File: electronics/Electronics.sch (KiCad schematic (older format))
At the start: 34 parts, among them U1 DRV8243, U2 DRV8243, U3 DRV8243

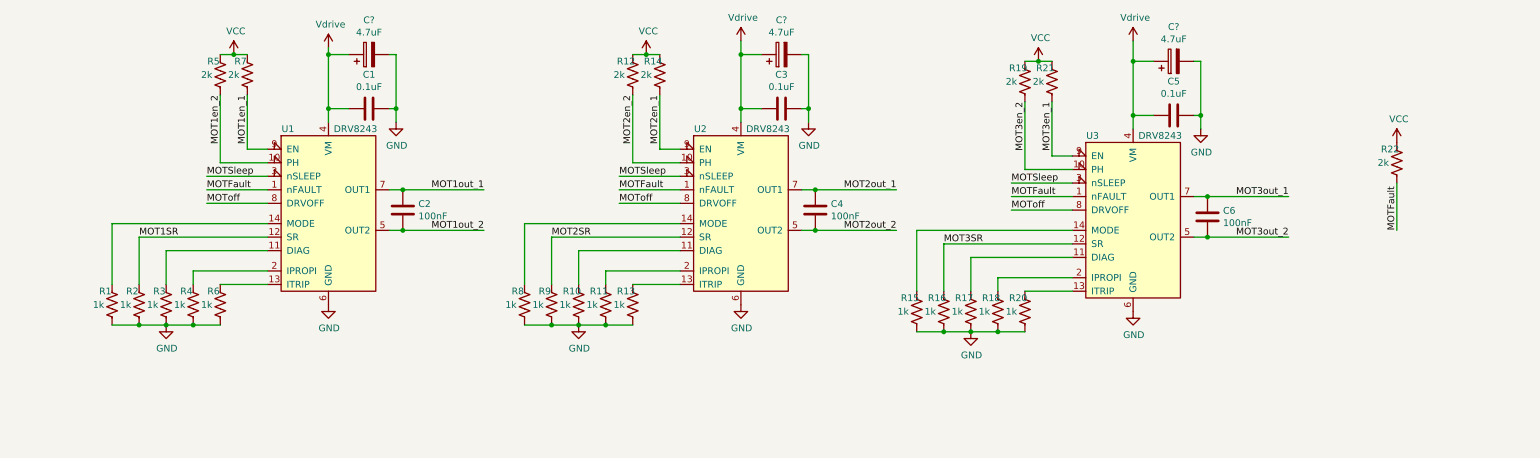
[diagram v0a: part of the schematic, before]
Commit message: Updated and removed unnecessary resistors, removed cache
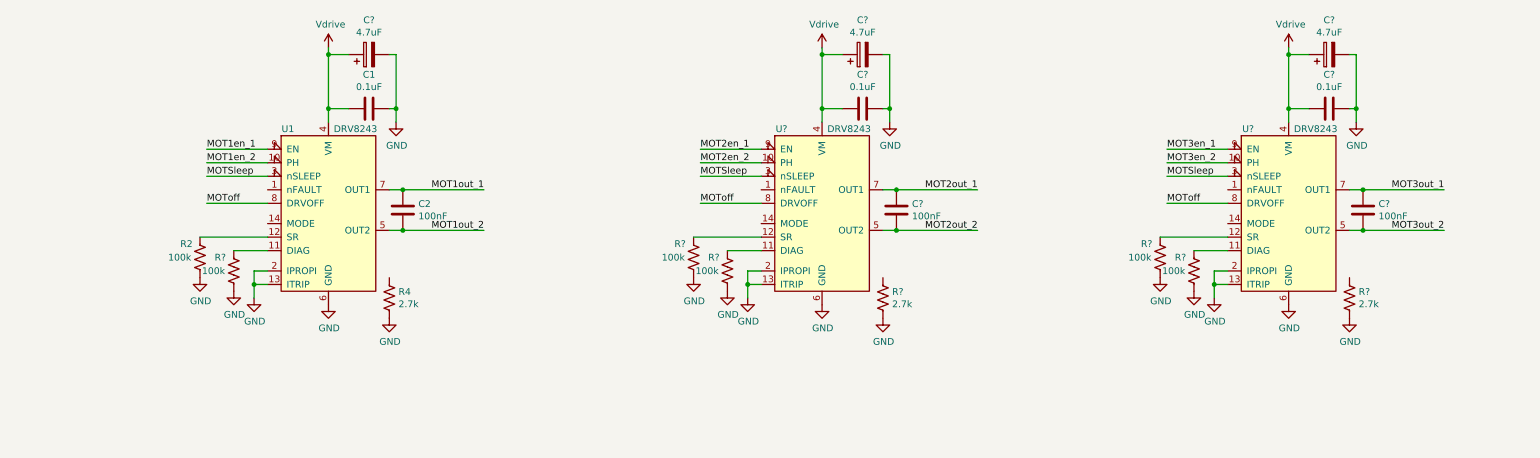
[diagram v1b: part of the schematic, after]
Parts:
- removed C3, C5: 0.1uF, Resistor_SMD:R_0603_1608Metric_Pad0.98x0.95mm_HandSolder, symbol Device:C
- removed C4, C6: 100nF, Resistor_SMD:R_0603_1608Metric_Pad0.98x0.95mm_HandSolder, symbol Device:C
- removed C? (x2): 4.7uF, symbol Device:CP
- removed R1, R10, R11, R13, R15, R16, R17, R18, R20, R3, R6, R8, R9: 1k, Resistor_SMD:R_0603_1608Metric_Pad0.98x0.95mm_HandSolder, symbol Device:R_US
- removed R12, R14, R19, R21, R22, R5, R7: 2k, Resistor_SMD:R_0603_1608Metric_Pad0.98x0.95mm_HandSolder, symbol Device:R_US
- removed U2, U3: DRV8243, Electronics:VQFN-HR-14, symbol Electronics:DRV8243
- added C? (x2): 0.1uF, Capacitor_SMD:C_0603_1608Metric_Pad1.08x0.95mm_HandSolder, symbol Device:C
- added C? (x2): 100nF, Resistor_SMD:R_0603_1608Metric_Pad0.98x0.95mm_HandSolder, symbol Device:C
- added C? (x2): 4.7uF, symbol Device:CP
- added R? (x5): 100k, Resistor_SMD:R_0603_1608Metric_Pad0.98x0.95mm_HandSolder, symbol Device:R_US
- added R? (x2): 2.7k, Resistor_SMD:R_0603_1608Metric_Pad0.98x0.95mm_HandSolder, symbol Device:R_US
- added U? (x2): DRV8243, Electronics:VQFN-HR-14, symbol Electronics:DRV8243
- R2: value 1k -> 100k
- R4: value 1k -> 2.7k
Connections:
- net GND: now also U1.13 (ITRIP), U1.2 (IPROPI), C?.1, C?.1, C?.2, C?.2, R?.2, R?.2, R?.2, R?.2, R?.2, R?.2, R?.2, U?.13 (ITRIP), U?.13 (ITRIP), U?.2 (IPROPI), U?.2 (IPROPI), U?.6 (GND), U?.6 (GND)
- net MOT2en_1: now also U?.9 (EN)
- net MOT2en_2: now also U?.10 (PH)
- net MOT2out_1: now also C?.1, U?.7 (OUT1)
- net MOT2out_2: now also C?.2, U?.5 (OUT2)
- net MOT3en_1: now also U?.9 (EN)
- net MOT3en_2: now also U?.10 (PH)
- net MOT3out_1: now also C?.1, U?.7 (OUT1)
- net MOT3out_2: now also C?.2, U?.5 (OUT2)
- net MOTSleep: now also U?.3 (nSLEEP), U?.3 (nSLEEP)
- net MOToff: now also U?.8 (DRVOFF), U?.8 (DRVOFF)
- net Vdrive: now also C?.1, C?.1, C?.2, C?.2, U?.4 (VM), U?.4 (VM)
- net at U1.11 (DIAG): now also R?.1
- net at R4.1: no longer U1.2 (IPROPI)
- net MOT1SR: no longer names the net of R2.1, U1.12 (SR)
- net MOTFault: no longer names the net of U1.1 (nFAULT)
- new net: R?.1, U?.12 (SR) (x2)
- new net: R?.1, U?.11 (DIAG) (x2)
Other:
- moved on the sheet: R2, R4

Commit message: Reorganised schematics, added regulators
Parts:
- removed C1, C? (x2): 0.1uF, Capacitor_SMD:C_0603_1608Metric_Pad1.08x0.95mm_HandSolder, symbol Device:C
- removed C2, C? (x2): 100nF, Resistor_SMD:R_0603_1608Metric_Pad0.98x0.95mm_HandSolder, symbol Device:C
- removed C? (x3): 4.7uF, symbol Device:CP
- removed R2, R? (x5): 100k, Resistor_SMD:R_0603_1608Metric_Pad0.98x0.95mm_HandSolder, symbol Device:R_US
- removed R4, R? (x2): 2.7k, Resistor_SMD:R_0603_1608Metric_Pad0.98x0.95mm_HandSolder, symbol Device:R_US
- removed U1, U? (x2): DRV8243, Electronics:VQFN-HR-14, symbol Electronics:DRV8243

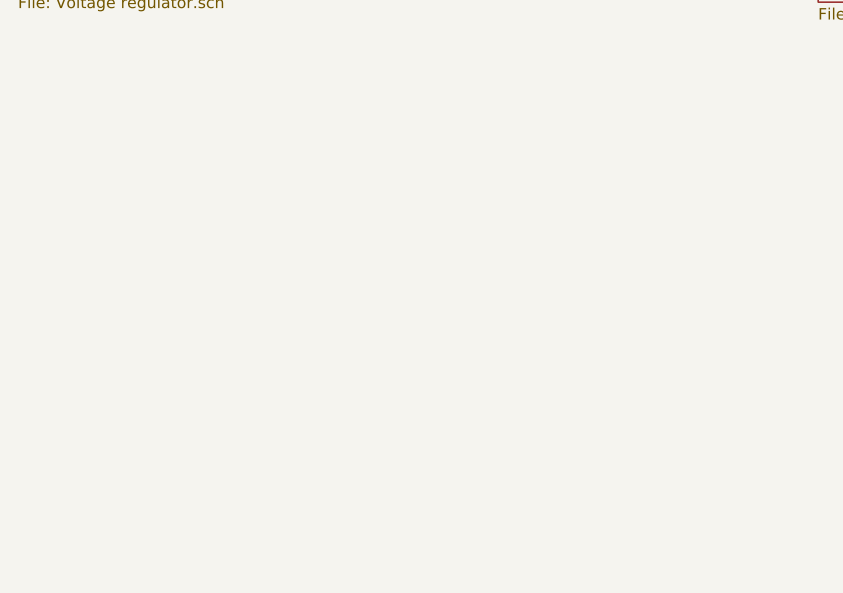
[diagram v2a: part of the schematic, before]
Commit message: Added connectors, started relabeling pins
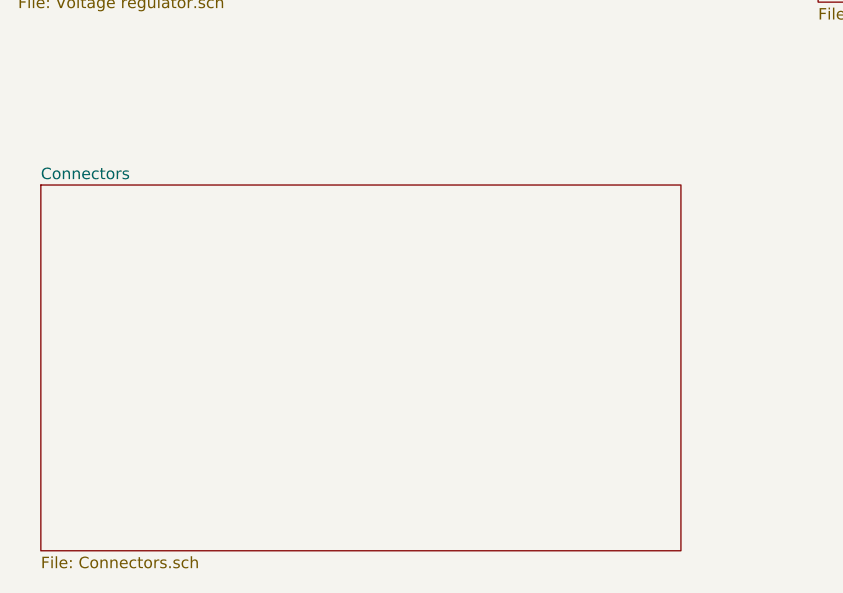
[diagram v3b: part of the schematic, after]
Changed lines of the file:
@@
 $Descr A4 11693 8268
 encoding utf-8
-Sheet 1 4
+Sheet 1 5
 Title ""
 Date ""
@@
 F1 "Voltage regulator.sch" 50
 $EndSheet
+$Sheet
+S 900  3650 2800 1600
+U 617B7795
+F0 "Connectors" 50
+F1 "Connectors.sch" 50
+$EndSheet
 $EndSCHEMATC

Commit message: Another restructure, added CPU pins, updated V regulators
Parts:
- added C? (x8): 0.1uF, symbol Device:C
- added C?: 4.7uF, symbol Device:CP
- added U?: STM32G441KBT3, LQFP32_7X7_STM, symbol 2021-09-13_09-53-18:STM32G441KBT3
- added U? (x3): MAX14930DASE+, 21-0041_S16+1_MXM, symbol MAX14930DASE+:MAX14930DASE+
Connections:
- net labels added: +3V3, +5VD, Aim-serv_PWM, Earth, GND, Hold-serv_PWM, MCU-Aim-serv_PWM, MCU-Hold-serv_PWM, MCU-MOT1en1, MCU-MOT1en2, MCU-MOT2en1, MCU-MOT2en2, MCU-MOT3en1, MCU-MOT3en2, MCU-TRW_PWM, MCU-USB_DM, MCU-USB_DP, MCU-mot1-enc_1, MCU-mot1-enc_2, MCU-mot2-enc_1, MCU-mot2-enc_2, MCU-mot3-enc_1, MCU-mot3-enc_2, MCU-mot_off, MCU-mot_sleep, MCU_NRST, MCU_SWCLK, MCU_SWDIO, MOT1en_1, MOT1en_2, MOT2en_1, MOT2en_2, MOT3en_1, MOT3en_2, MOT_off, MOT_sleep, TRW_PWM
- wire segments 0 -> 77

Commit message: Updated titles
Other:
- note added: "1.0"
- note added: "21/10/2021"
- note added: "CPU and isolators"
- note added: "Link to Hbridges"
- note added: "Link to all connectors and voltage regulators"
- note added: "Motor 1 and 2 PWM isolator"
- note added: "Motor 3 PWM, DC motors sleep and off control isolator"
- note added: "STM32G4 MCU"
- note added: "Thrower and servo control PWM isolator"
- moved on the sheet: C?

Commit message: Added debug LEDs
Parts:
- added D? (x2): RED_LED, symbol Device:LED
- added D? (x2): GREEN_LED, symbol Device:LED
- added R? (x4): 3.3k, symbol Device:R
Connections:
- net labels added: MCU-MOT1en_1, MCU-MOT1en_2, MCU-MOT2en_1, MCU-MOT2en_2, MCU-MOT3en_1, MCU-MOT3en_2, MCU-debug-LED_1, MCU-debug-LED_2, MCU-debug-LED_3, MCU-debug-LED_4
- net labels removed: MCU-MOT1en1, MCU-MOT1en2, MCU-MOT2en1, MCU-MOT2en2, MCU-MOT3en1, MCU-MOT3en2
- wire segments 77 -> 85
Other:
- note added: "Debug LED 1"
- note added: "Debug LED 2"
- note added: "Debug LED 3"
- note added: "Debug LED 4"

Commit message: Removed redundant comments
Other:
- note added: "Debug LEDs"
- note removed: "Debug LED 1"
- note removed: "Debug LED 2"
- note removed: "Debug LED 3"
- note removed: "Debug LED 4"
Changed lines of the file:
@@
 	0    1    1    0
 $EndComp
-Text Notes 1300 4950 0    50   ~ 0
-Debug LED 1
 $Comp
 L power:GND #PWR?
@@
 L Device:LED D?
 U 1 1 61754D02
-P 1700 5400
+P 1700 5250
 AR Path="/61754D02" Ref="D?"  Part="1"
 AR Path="/617B7795/61754D02" Ref="D?"  Part="1"
-F 0 "D?" H 1693 5145 50  0000 C CNN
-F 1 "RED_LED" H 1693 5236 50  0000 C CNN
-F 2 "" H 1700 5400 50  0001 C CNN
-F 3 "~" H 1700 5400 50  0001 C CNN
-	1    1700 5400
+F 0 "D?" H 1693 4995 50  0000 C CNN
+F 1 "RED_LED" H 1693 5086 50  0000 C CNN
+F 2 "" H 1700 5250 50  0001 C CNN
+F 3 "~" H 1700 5250 50  0001 C CNN
+	1    1700 5250
 	-1   0    0    1
 $EndComp
@@
 L Device:R R?
 U 1 1 61754D08
-P 2050 5400
+P 2050 5250
 AR Path="/615F51F3/61754D08" Ref="R?"  Part="1"
 AR Path="/617B7795/61754D08" Ref="R?"  Part="1"
 AR Path="/61754D08" Ref="R?"  Part="1"
-F 0 "R?" V 1800 5400 50  0000 C CNN
-F 1 "3.3k" V 1900 5400 50  0000 C CNN
-F 2 "" V 1980 5400 50  0001 C CNN
-F 3 "~" H 2050 5400 50  0001 C CNN
-	1    2050 5400
+F 0 "R?" V 1800 5250 50  0000 C CNN
+F 1 "3.3k" V 1900 5250 50  0000 C CNN
+F 2 "" V 1980 5250 50  0001 C CNN
+F 3 "~" H 2050 5250 50  0001 C CNN
+	1    2050 5250
 	0    1    1    0
 $EndComp
-Text Notes 1350 5650 0    50   ~ 0
-Debug LED 2
 $Comp
 L power:GND #PWR?
 U 1 1 61754D0F
-P 2200 5400
+P 2200 5250
 AR Path="/615F51F3/61754D0F" Ref="#PWR?"  Part="1"
 AR Path="/617B7795/61754D0F" Ref="#PWR?"  Part="1"
 AR Path="/61754D0F" Ref="#PWR?"  Part="1"
-F 0 "#PWR?" H 2200 5150 50  0001 C CNN
-F 1 "GND" H 2205 5227 50  0000 C CNN
-F 2 "" H 2200 5400 50  0001 C CNN
-F 3 "" H 2200 5400 50  0001 C CNN
-	1    2200 5400
+F 0 "#PWR?" H 2200 5000 50  0001 C CNN
+F 1 "GND" H 2205 5077 50  0000 C CNN
+F 2 "" H 2200 5250 50  0001 C CNN
+F 3 "" H 2200 5250 50  0001 C CNN
+	1    2200 5250
 	1    0    0    -1
 $EndComp
 Wire Wire Line
-	1850 5400 1900 5400
+	1850 5250 1900 5250
 $Comp
 L Device:LED D?
@@
 	0    1    1    0
 $EndComp
-Text Notes 2800 4950 0    50   ~ 0
-Debug LED 3
 $Comp
 L power:GND #PWR?
@@
 L Device:LED D?
 U 1 1 61778BA0
-P 3200 5400
+P 3200 5250
 AR Path="/61778BA0" Ref="D?"  Part="1"
 AR Path="/617B7795/61778BA0" Ref="D?"  Part="1"
-F 0 "D?" H 3193 5145 50  0000 C CNN
-F 1 "GREEN_LED" H 3193 5236 50  0000 C CNN
-F 2 "" H 3200 5400 50  0001 C CNN
-F 3 "~" H 3200 5400 50  0001 C CNN
-	1    3200 5400
+F 0 "D?" H 3193 4995 50  0000 C CNN
+F 1 "GREEN_LED" H 3193 5086 50  0000 C CNN
+F 2 "" H 3200 5250 50  0001 C CNN
+F 3 "~" H 3200 5250 50  0001 C CNN
+	1    3200 5250
 	-1   0    0    1
 $EndComp
@@
 L Device:R R?
 U 1 1 61778BA6
-P 3550 5400
+P 3550 5250
 AR Path="/615F51F3/61778BA6" Ref="R?"  Part="1"
 AR Path="/617B7795/61778BA6" Ref="R?"  Part="1"
 AR Path="/61778BA6" Ref="R?"  Part="1"
-F 0 "R?" V 3300 5400 50  0000 C CNN
-F 1 "3.3k" V 3400 5400 50  0000 C CNN
-F 2 "" V 3480 5400 50  0001 C CNN
-F 3 "~" H 3550 5400 50  0001 C CNN
-	1    3550 5400
+F 0 "R?" V 3300 5250 50  0000 C CNN
+F 1 "3.3k" V 3400 5250 50  0000 C CNN
+F 2 "" V 3480 5250 50  0001 C CNN
+F 3 "~" H 3550 5250 50  0001 C CNN
+	1    3550 5250
 	0    1    1    0
 $EndComp
-Text Notes 2800 5650 0    50   ~ 0
-Debug LED 4
+Text Notes 2050 5650 0    50   ~ 0
+Debug LEDs
 $Comp
 L power:GND #PWR?
 U 1 1 61778BAD
-P 3700 5400
+P 3700 5250
 AR Path="/615F51F3/61778BAD" Ref="#PWR?"  Part="1"
 AR Path="/617B7795/61778BAD" Ref="#PWR?"  Part="1"
 AR Path="/61778BAD" Ref="#PWR?"  Part="1"
-F 0 "#PWR?" H 3700 5150 50  0001 C CNN
-F 1 "GND" H 3705 5227 50  0000 C CNN
-F 2 "" H 3700 5400 50  0001 C CNN
-F 3 "" H 3700 5400 50  0001 C CNN
-	1    3700 5400
+F 0 "#PWR?" H 3700 5000 50  0001 C CNN
+F 1 "GND" H 3705 5077 50  0000 C CNN
+F 2 "" H 3700 5250 50  0001 C CNN
+F 3 "" H 3700 5250 50  0001 C CNN
+	1    3700 5250
 	1    0    0    -1
 $EndComp
 Wire Wire Line
-	3350 5400 3400 5400
+	3350 5250 3400 5250
 Text Label 700  2250 0    50   ~ 0
 MCU-debug-LED_3
@@
 Wire Wire Line
 	850  4700 1550 4700
-Text Label 850  5400 0    50   ~ 0
+Text Label 850  5250 0    50   ~ 0
 MCU-debug-LED_2
 Wire Wire Line
-	850  5400 1550 5400
-Text Label 2350 5400 0    50   ~ 0
+	850  5250 1550 5250
+Text Label 2350 5250 0    50   ~ 0
 MCU-debug-LED_4
 Wire Wire Line
-	2350 5400 3050 5400
+	2350 5250 3050 5250
 Text Label 2350 4700 0    50   ~ 0
 MCU-debug-LED_3
